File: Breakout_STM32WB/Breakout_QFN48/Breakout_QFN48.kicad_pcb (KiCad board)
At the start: 4 copper layers, 72 parts, among them J1 Debug conn, J10 Conn_01x01, J11 Conn_01x01, J12 Conn_01x01, J13 Conn_01x01, J14 Conn_01x01, J15 Conn_01x01, J16 Conn_01x01, J17 Conn_01x01, J18 Conn_01x01, J19 Conn_01x01, J2 Conn_01x01, J20 Conn_01x01, J21 Conn_01x01, J22 Conn_01x01, J23 Conn_01x01, J24 Conn_01x01, J25 Conn_01x01, J26 Conn_01x01, J27 Conn_01x01, J28 Conn_01x01, J29 RF_Shield_One_Piece, J3 Conn_01x01, J30 Conn_01x01, J31 Conn_01x01, J32 Conn_01x01, J33 Conn_01x01, J34 Conn_01x01, J35 Conn_01x01, J36 Conn_01x01, J37 Conn_01x01, J38 Conn_01x01, J39 Conn_01x01, J4 Conn_01x01, J40 Conn_01x01, J5 Conn_01x01, J6 Conn_01x01, J7 Conn_01x01, J8 Conn_01x01, J9 Conn_01x01, U1 STM32WB55Cx, U2 LFL212G45TC1A007, U3 MCP1700-3302E_SOT23, Y1 NX2012SA_32-768kHz, Y2 NX2016_32M

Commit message: update layout
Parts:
- moved C12 37.0 mm to (113.6, 94.4)
- moved Y2 36.4 mm to (110.8, 95.9), turned to 180 degrees
- moved AE1 35.3 mm to (110.2, 85.3)
- moved U2 35.0 mm to (114.9, 88.5), turned to 90 degrees
- moved C13 32.2 mm to (114.5, 93.5), turned to 180 degrees
- moved C5 27.7 mm to (111.3, 103.1), turned to 270 degrees
- moved C14 26.9 mm to (114.4, 90.7), turned to 180 degrees
- moved C11 22.5 mm to (113.6, 95.3)
- moved C10 22.1 mm to (121.8, 99.3)
- moved C8 21.6 mm to (123.4, 102.0), turned to 270 degrees
- moved L3 20.9 mm to (121.8, 98.3)
- moved C6 17.1 mm to (119.9, 105.0)
- moved Y1 14.7 mm to (122.2, 102.4), turned to 270 degrees
- moved C4 14.6 mm to (123.5, 103.9), turned to 90 degrees
- moved C2 14.5 mm to (115.5, 105.0)
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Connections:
- Y2 pad 2: Net-(Y2-Pad2) -> GND
- Y2 pad 4: Net-(Y2-Pad4) -> GND
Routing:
- net Net-(C11-Pad1): track 6.34 -> 2.88 mm, vias 2 -> 0
- net Net-(U1-Pad25): track 0.00 -> 3.44 mm
- net GND: track 0.00 -> 2.69 mm
- net Net-(U1-Pad24): track 1.55 -> 3.02 mm

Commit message: update layout
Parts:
- C10, C11, C12, C13, C14, C15, C16, C17, C18, C2, C3, C4, C5, C6, C8, C9: footprint Capacitor_SMD:C_0402_1005Metric -> Yame_library:SM0201-MR
- JP1: footprint Jumper:SolderJumper-2_P1.3mm_Open_TrianglePad1.0x1.5mm -> Yame_library:SolderJumper-2_Open_TrianglePad1.0x1.0mm
- L3: value 10nH -> Ferrite beads 0603; footprint Inductor_SMD:L_0402_1005Metric -> Yame_library:SM0603-MR
- L4, L5: footprint Inductor_SMD:L_0402_1005Metric -> Yame_library:SM0201-MR
- moved RF_J1 34.7 mm to (109.0, 90.0), turned to 180 degrees
- moved C18 10.1 mm to (111.7, 90.3), turned to 180 degrees
- moved L5 9.03 mm to (112.0, 91.2), turned to 90 degrees
- moved C17 8.36 mm to (111.8, 92.3), turned to 270 degrees
- moved U2 3.74 mm to (113.8, 92.1), turned to 180 degrees
- moved C14 3.02 mm to (114.7, 93.7)
- moved L4 2.45 mm to (115.0, 94.5)
- moved JP1 1.95 mm to (109.8, 101.0)
- moved C13 1.88 mm to (114.7, 95.3)
- moved AE1 1.75 mm to (112.0, 85.6)
- moved L2 1.25 mm to (107.9, 101.0), turned to 0 degrees
- moved C7 0.73 mm to (110.9, 99.4)
- moved C5 0.52 mm to (111.8, 102.8)
- moved L1 0.33 mm to (108.3, 99.5)
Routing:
- net Net-(J18-Pad1): track 0.00 -> 7.76 mm
- net Net-(J19-Pad1): track 0.00 -> 7.70 mm
- net Net-(J28-Pad1): track 0.00 -> 7.69 mm
- net Net-(JP1-Pad2): track 0.00 -> 5.37 mm
- net Net-(C1-Pad1): track 0.00 -> 4.42 mm
- net Net-(C7-Pad1): track 0.00 -> 3.83 mm
- net Net-(J14-Pad1): track 1.36 -> 5.08 mm, vias 1 -> 0
- net Net-(J16-Pad1): track 4.09 -> 6.45 mm
- net Net-(L1-Pad2): track 0.00 -> 1.50 mm
- net Net-(J15-Pad1): track 3.64 -> 4.70 mm
- net GND: track 2.69 -> 3.73 mm, vias 0 -> 3
- net +3V3: vias 0 -> 1
- net (no net): vias 3 -> 0
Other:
- net class Default: via_dia 0.4 -> 0.6; via_drill 0.2 -> 0.3

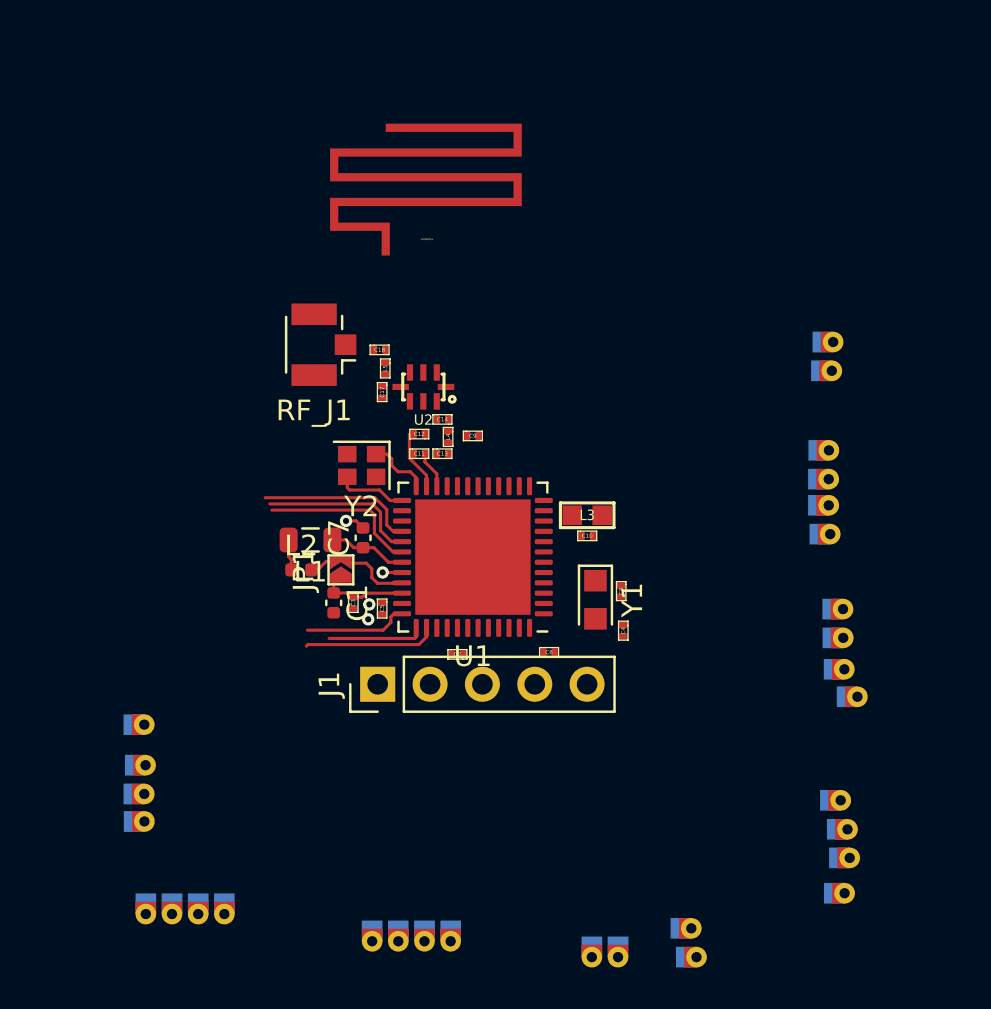
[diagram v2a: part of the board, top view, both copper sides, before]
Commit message: Breakout_STM32WB : update layout
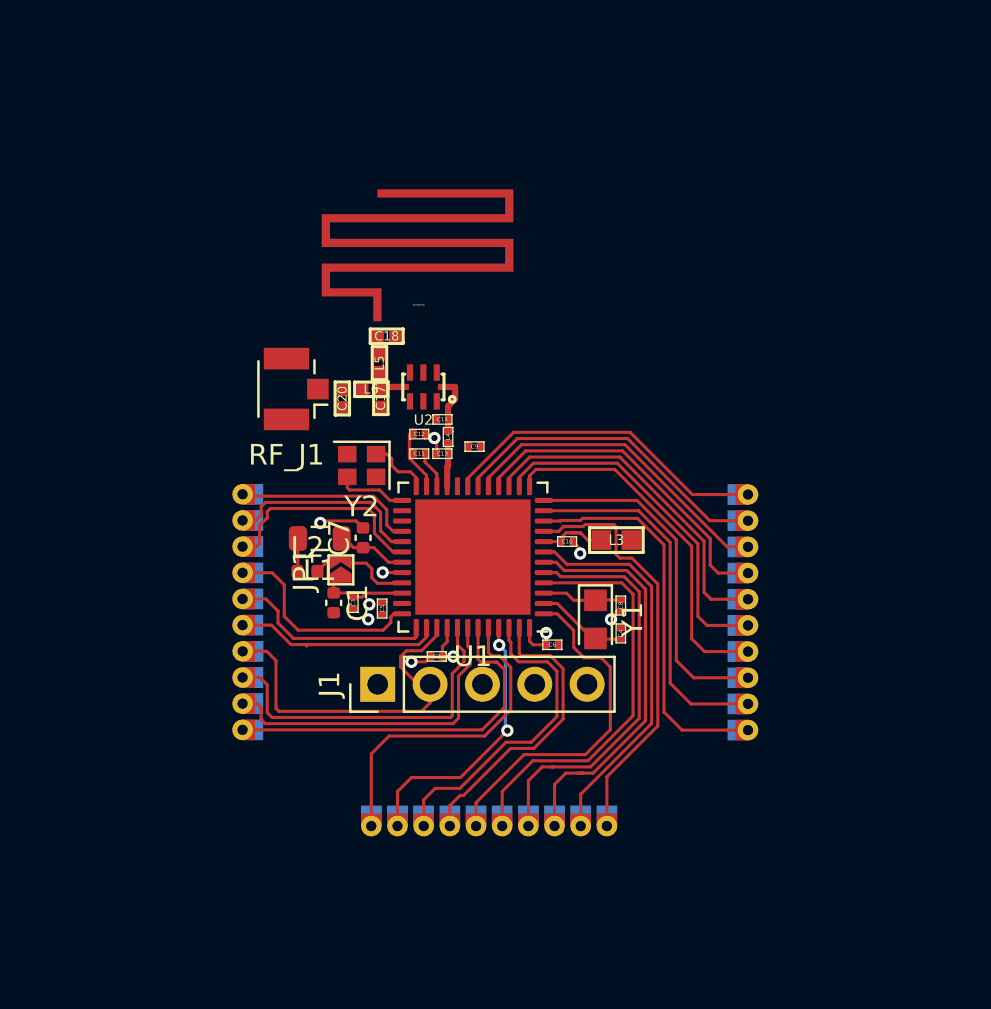
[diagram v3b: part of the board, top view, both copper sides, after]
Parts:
- added C20: 100n, Yame_library:SM0402-MR, F.Cu at (109.9, 92.6)
- added L6: L, Yame_library:SM0402-MR, F.Cu at (111.3, 92.2)
- C17, C18, L5: footprint Yame_library:SM0201-MR -> Yame_library:SM0402-MR
- moved J15 16.0 mm to (105.0, 102.4), turned to 180 degrees
- moved J26 15.7 mm to (118.9, 113.4), turned to 270 degrees
- moved J16 14.4 mm to (105.0, 103.6), turned to 180 degrees
- moved J27 14.4 mm to (120.2, 113.4), turned to 270 degrees
- moved J17 13.1 mm to (105.0, 107.4), turned to 180 degrees
- moved J14 13.0 mm to (105.0, 101.1), turned to 180 degrees
- moved J30 12.9 mm to (121.4, 113.4), turned to 270 degrees
- moved J39 12.9 mm to (105.0, 104.9), turned to 180 degrees
- moved J28 12.9 mm to (105.0, 99.8), turned to 180 degrees
- moved J19 12.8 mm to (105.0, 98.6), turned to 180 degrees
- moved J21 12.7 mm to (105.0, 108.7), turned to 180 degrees
- moved J2 12.4 mm to (116.4, 113.4), turned to 270 degrees
- moved J18 12.2 mm to (105.0, 97.3), turned to 180 degrees
- moved J40 11.5 mm to (105.0, 106.2), turned to 180 degrees
- moved J4 11.4 mm to (122.7, 113.4), turned to 270 degrees
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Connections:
- RF_J1 pad 1: Net-(AE1-Pad1) -> Net-(C20-Pad1)
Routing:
- net Net-(J4-Pad1): track 0.00 -> 20.4 mm
- net Net-(J27-Pad1): track 0.00 -> 19.8 mm
- net Net-(J26-Pad1): track 0.00 -> 19.8 mm
- net Net-(J3-Pad1): track 0.00 -> 19.7 mm
- net /NRST: track 0.00 -> 19.0 mm
- net Net-(J5-Pad1): track 0.00 -> 19.0 mm
- net Net-(J21-Pad1): track 0.00 -> 18.1 mm
- net Net-(J6-Pad1): track 0.00 -> 17.8 mm
- net Net-(J8-Pad1): track 0.00 -> 17.5 mm
- net /SWDIO: track 0.00 -> 17.3 mm
- net Net-(J9-Pad1): track 0.00 -> 17.1 mm
- net Net-(J2-Pad1): track 0.00 -> 16.9 mm
- net Net-(J7-Pad1): track 0.00 -> 16.9 mm
- net Net-(J10-Pad1): track 0.00 -> 16.7 mm
- net /SWDCLK: track 0.00 -> 16.4 mm
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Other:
- rule via_min_size: 0.4 -> 0.6

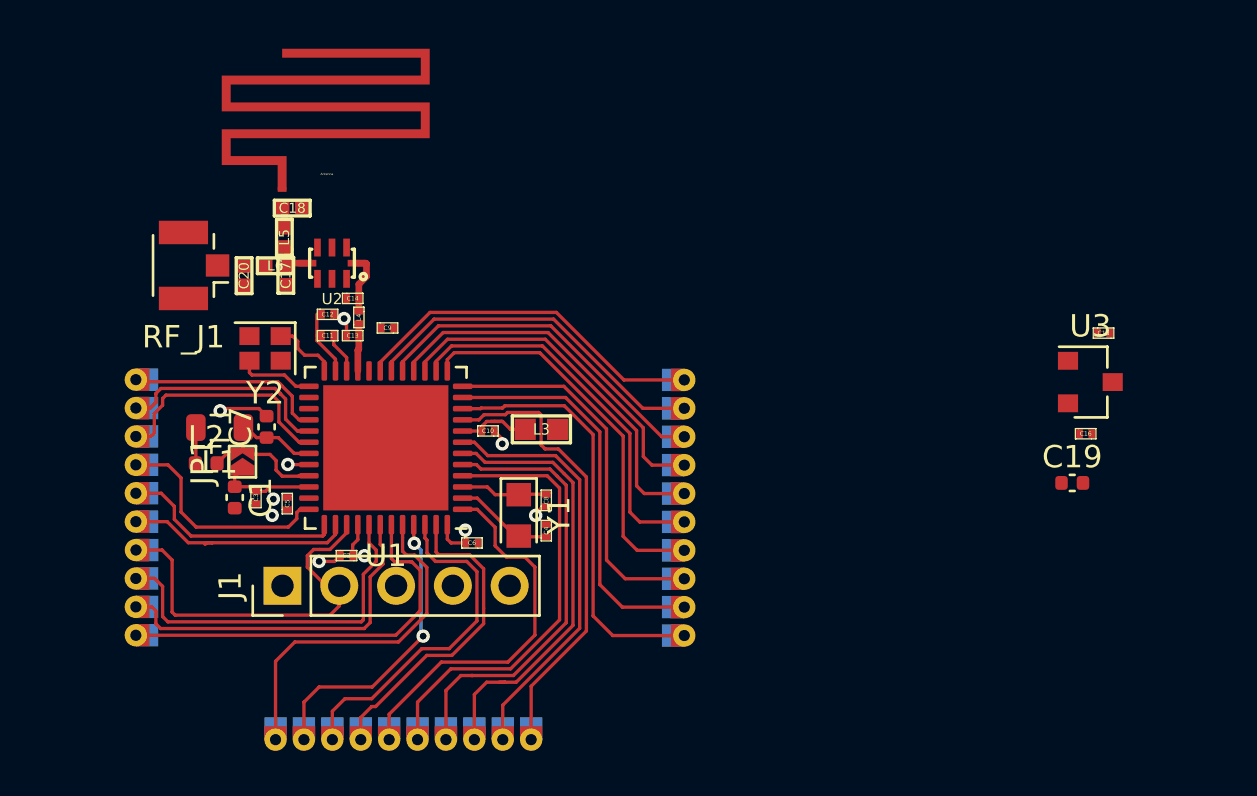
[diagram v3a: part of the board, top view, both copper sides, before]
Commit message: Breakout_STM32WB : Update layout
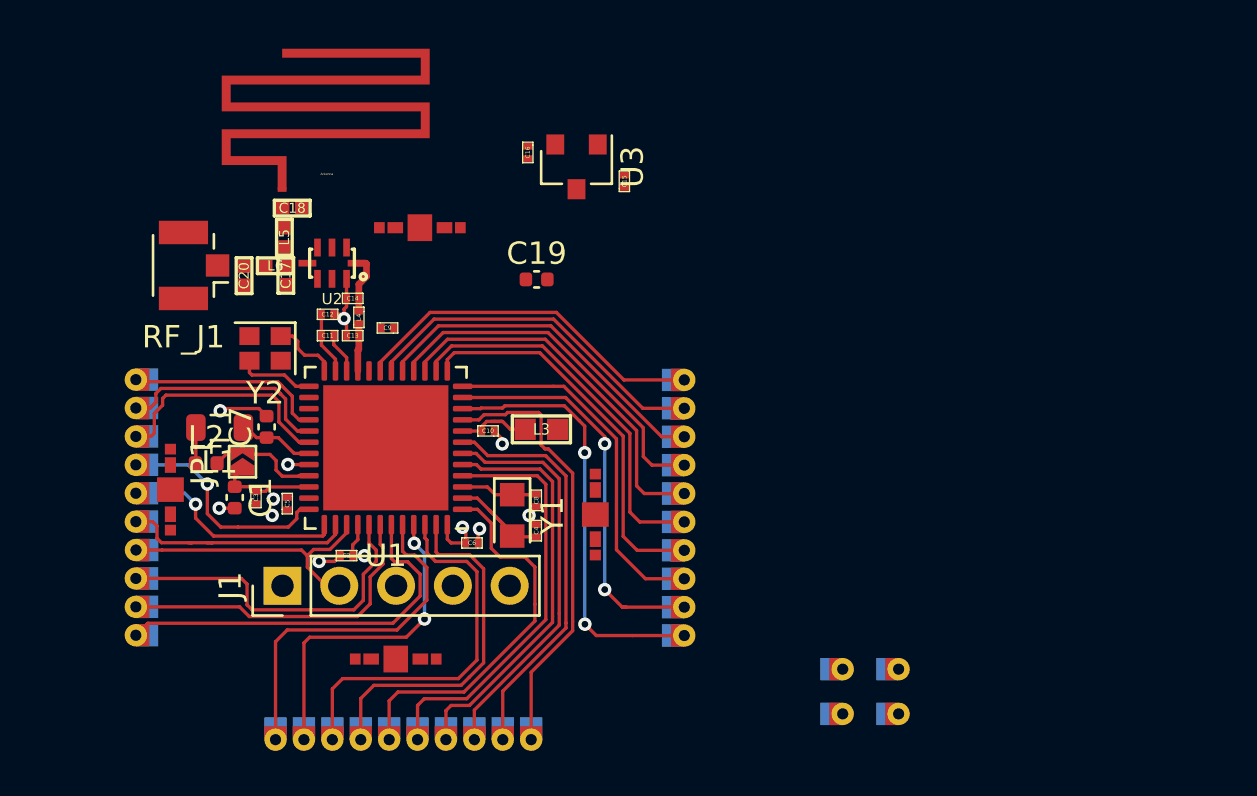
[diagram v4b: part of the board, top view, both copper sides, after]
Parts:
- added J41: Conn_01x01, Yame_library:Castellated, F.Cu at (136.6, 110.2)
- added J42: Conn_01x01, Yame_library:Castellated, F.Cu at (136.6, 112.2)
- added J43: Conn_01x01, Yame_library:Castellated, F.Cu at (139.1, 110.2)
- added J44: Conn_01x01, Yame_library:Castellated, F.Cu at (139.1, 112.2)
- added J45: Conn_01x01, Yame_library:S0951-46R, F.Cu at (117.7, 90.5)
- added J46: Conn_01x01, Yame_library:S0951-46R, F.Cu at (106.6, 102.2)
- added J47: Conn_01x01, Yame_library:S0951-46R, F.Cu at (125.6, 103.3)
- added J48: Conn_01x01, Yame_library:S0951-46R, F.Cu at (116.7, 109.8)
- moved C16 27.9 mm to (122.6, 87.1), turned to 270 degrees
- moved C19 25.6 mm to (123.0, 92.8)
- moved U3 24.9 mm to (124.7, 87.8), turned to 270 degrees
- moved C15 22.5 mm to (126.9, 88.4), turned to 90 degrees
- moved C4 0.44 mm to (122.9, 104.0)
- moved C8 0.44 mm to (122.9, 102.7)
- moved Y1 0.29 mm to (121.9, 103.4)
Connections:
- J1 pad 1: /NRST -> +3V3
- J1 pad 5: +3V3 -> /NRST
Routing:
- net /SWDIO: track 17.3 -> 12.3 mm
- net GND: track 8.43 -> 12.5 mm, vias 7 -> 9
- net Net-(J27-Pad1): track 19.8 -> 17.7 mm
- net Net-(J25-Pad1): track 14.0 -> 15.9 mm
- net Net-(J26-Pad1): track 19.8 -> 18.0 mm
- net Net-(J24-Pad1): track 15.2 -> 16.8 mm
- net Net-(C17-Pad1): track 1.57 -> 0.00 mm
- net Net-(J17-Pad1): track 16.0 -> 14.4 mm
- net Net-(C4-Pad1): track 4.45 -> 5.92 mm
- net Net-(J3-Pad1): track 19.7 -> 18.5 mm
- net /SWDCLK: track 16.4 -> 15.2 mm
- net Net-(J23-Pad1): track 13.4 -> 14.6 mm
- net /NRST: track 19.0 -> 17.9 mm
- net Net-(J4-Pad1): track 20.4 -> 19.3 mm
- net Net-(AE1-Pad1): track 0.62 -> 0.00 mm
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
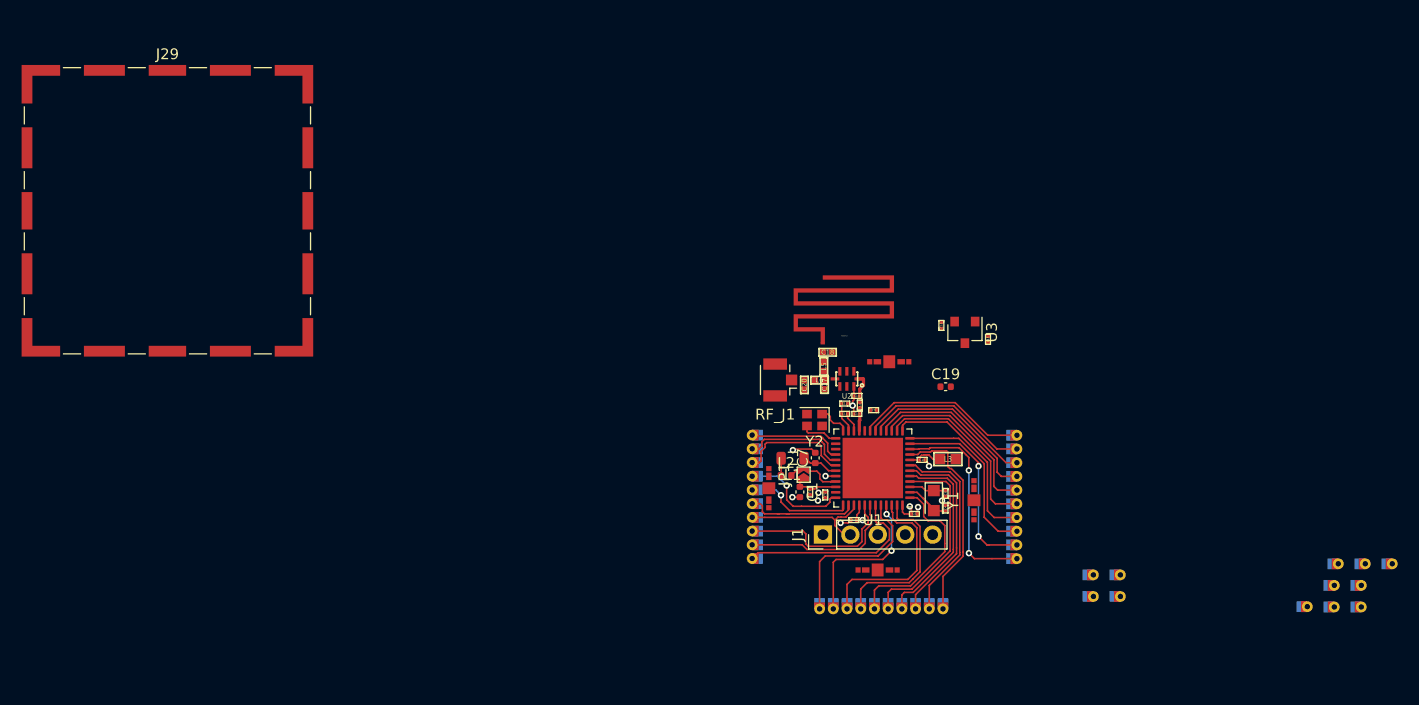
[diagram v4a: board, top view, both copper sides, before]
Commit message: Breakout_STM32WB : update layout
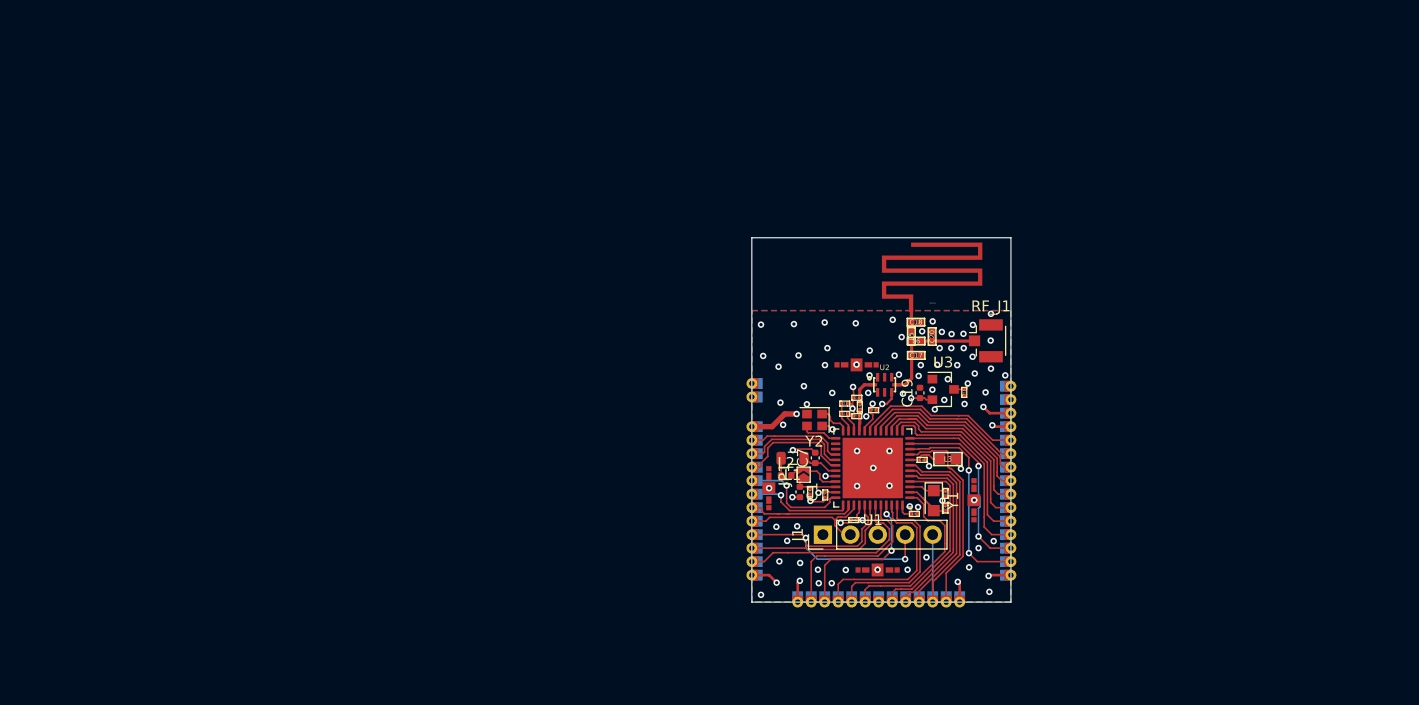
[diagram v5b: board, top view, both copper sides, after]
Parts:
- removed C16: 1u, Yame_library:SM0201-MR
- removed J29: RF_Shield_One_Piece, RF_Shielding:Laird_Technologies_BMI-S-203-F_26.21x26.21mm
- moved J38 60.1 mm to (105.0, 92.5), turned to 180 degrees
- moved J36 59.1 mm to (105.0, 93.8), turned to 180 degrees
- moved J31 55.8 mm to (105.0, 96.5), turned to 180 degrees
- moved J37 38.5 mm to (129.0, 94.0)
- moved J35 36.3 mm to (129.0, 92.8)
- moved J34 35.7 mm to (129.0, 95.2)
- moved J43 34.1 mm to (105.0, 110.2), turned to 180 degrees
- moved J33 33.4 mm to (129.0, 96.5)
- moved J44 29.9 mm to (109.2, 112.8), turned to 270 degrees
- moved J32 27.6 mm to (129.0, 110.2)
- moved J42 19.9 mm to (116.8, 112.8), turned to 270 degrees
- moved RF_J1 19.4 mm to (126.7, 88.5), turned to 0 degrees
- moved C20 12.7 mm to (121.7, 88.2), turned to 90 degrees
- moved J41 12.6 mm to (124.2, 112.8), turned to 270 degrees
- moved L6 9.66 mm to (120.2, 88.6), turned to 0 degrees
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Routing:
- net GND: track 12.5 -> 53.5 mm, vias 9 -> 91
- net +3V3: track 4.31 -> 30.7 mm, vias 3 -> 7
- net /SWDCLK: track 15.2 -> 27.4 mm, vias 0 -> 2
- net +5V: track 0.00 -> 9.77 mm, vias 0 -> 1
- net /NRST: track 17.9 -> 23.5 mm
- net Net-(C17-Pad1): track 0.00 -> 5.10 mm
- net Net-(C20-Pad1): track 0.00 -> 4.99 mm
- net Net-(AE1-Pad1): track 0.00 -> 1.96 mm
- net Net-(J3-Pad1): track 18.5 -> 17.5 mm
- net Net-(J27-Pad1): track 17.7 -> 17.0 mm
- net Net-(J26-Pad1): track 18.0 -> 17.3 mm
- net Net-(J13-Pad1): track 15.9 -> 15.3 mm
- net Net-(J20-Pad1): track 16.2 -> 15.5 mm
- added copper zone on PWR.Cu, net +3V3
- added copper zone on PWR.Cu, net +5V
- added copper zone on B.Cu, net GND
- added copper zone on F.Cu, net GND
- added copper zone on GND.Cu, net GND
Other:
- board outline added: 24 x 33.8 mm
